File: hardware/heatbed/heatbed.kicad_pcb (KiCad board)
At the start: 2 copper layers, 200 x 200 mm, 4 parts, among them J1 Conn_01x01, J2 Conn_01x01

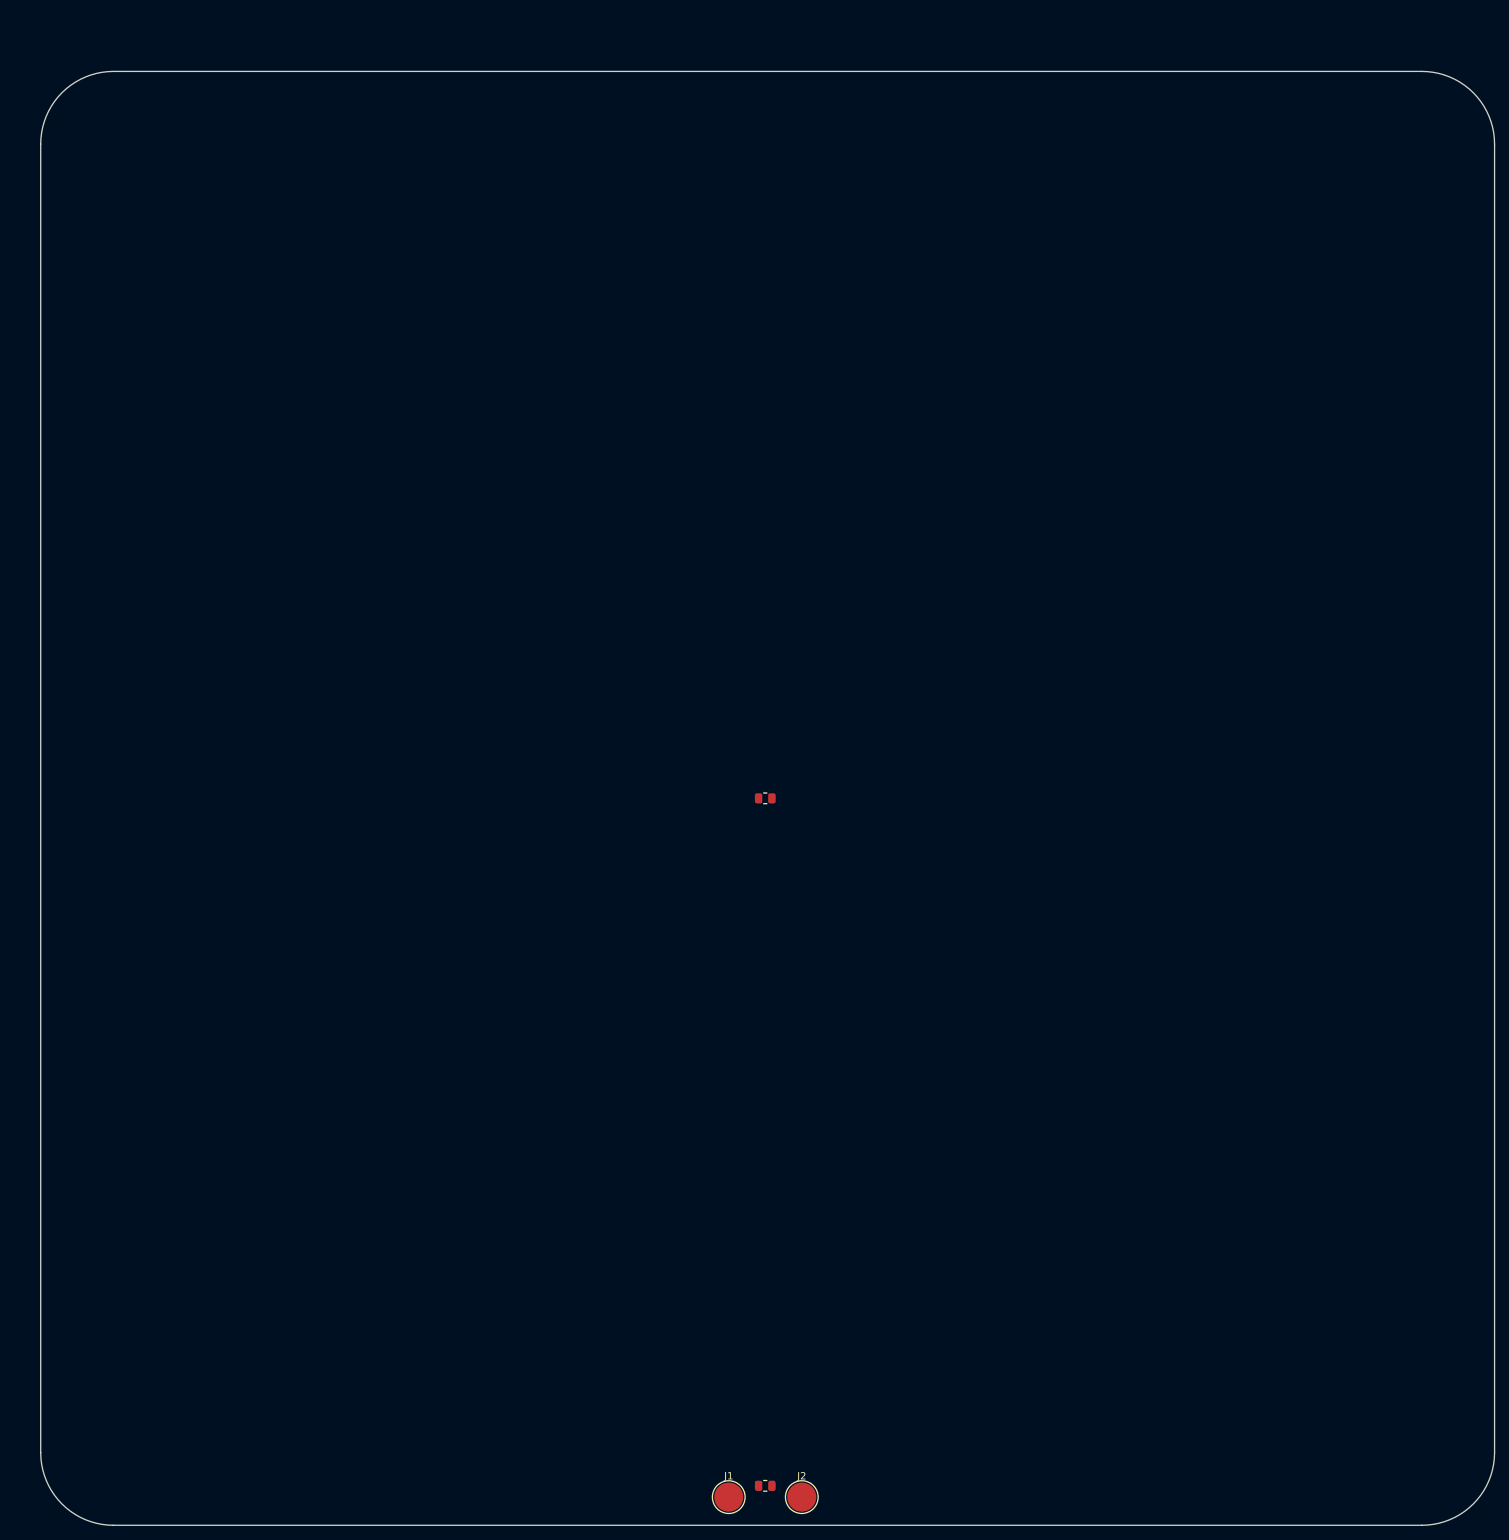
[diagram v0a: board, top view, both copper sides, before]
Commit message: add heatbed image
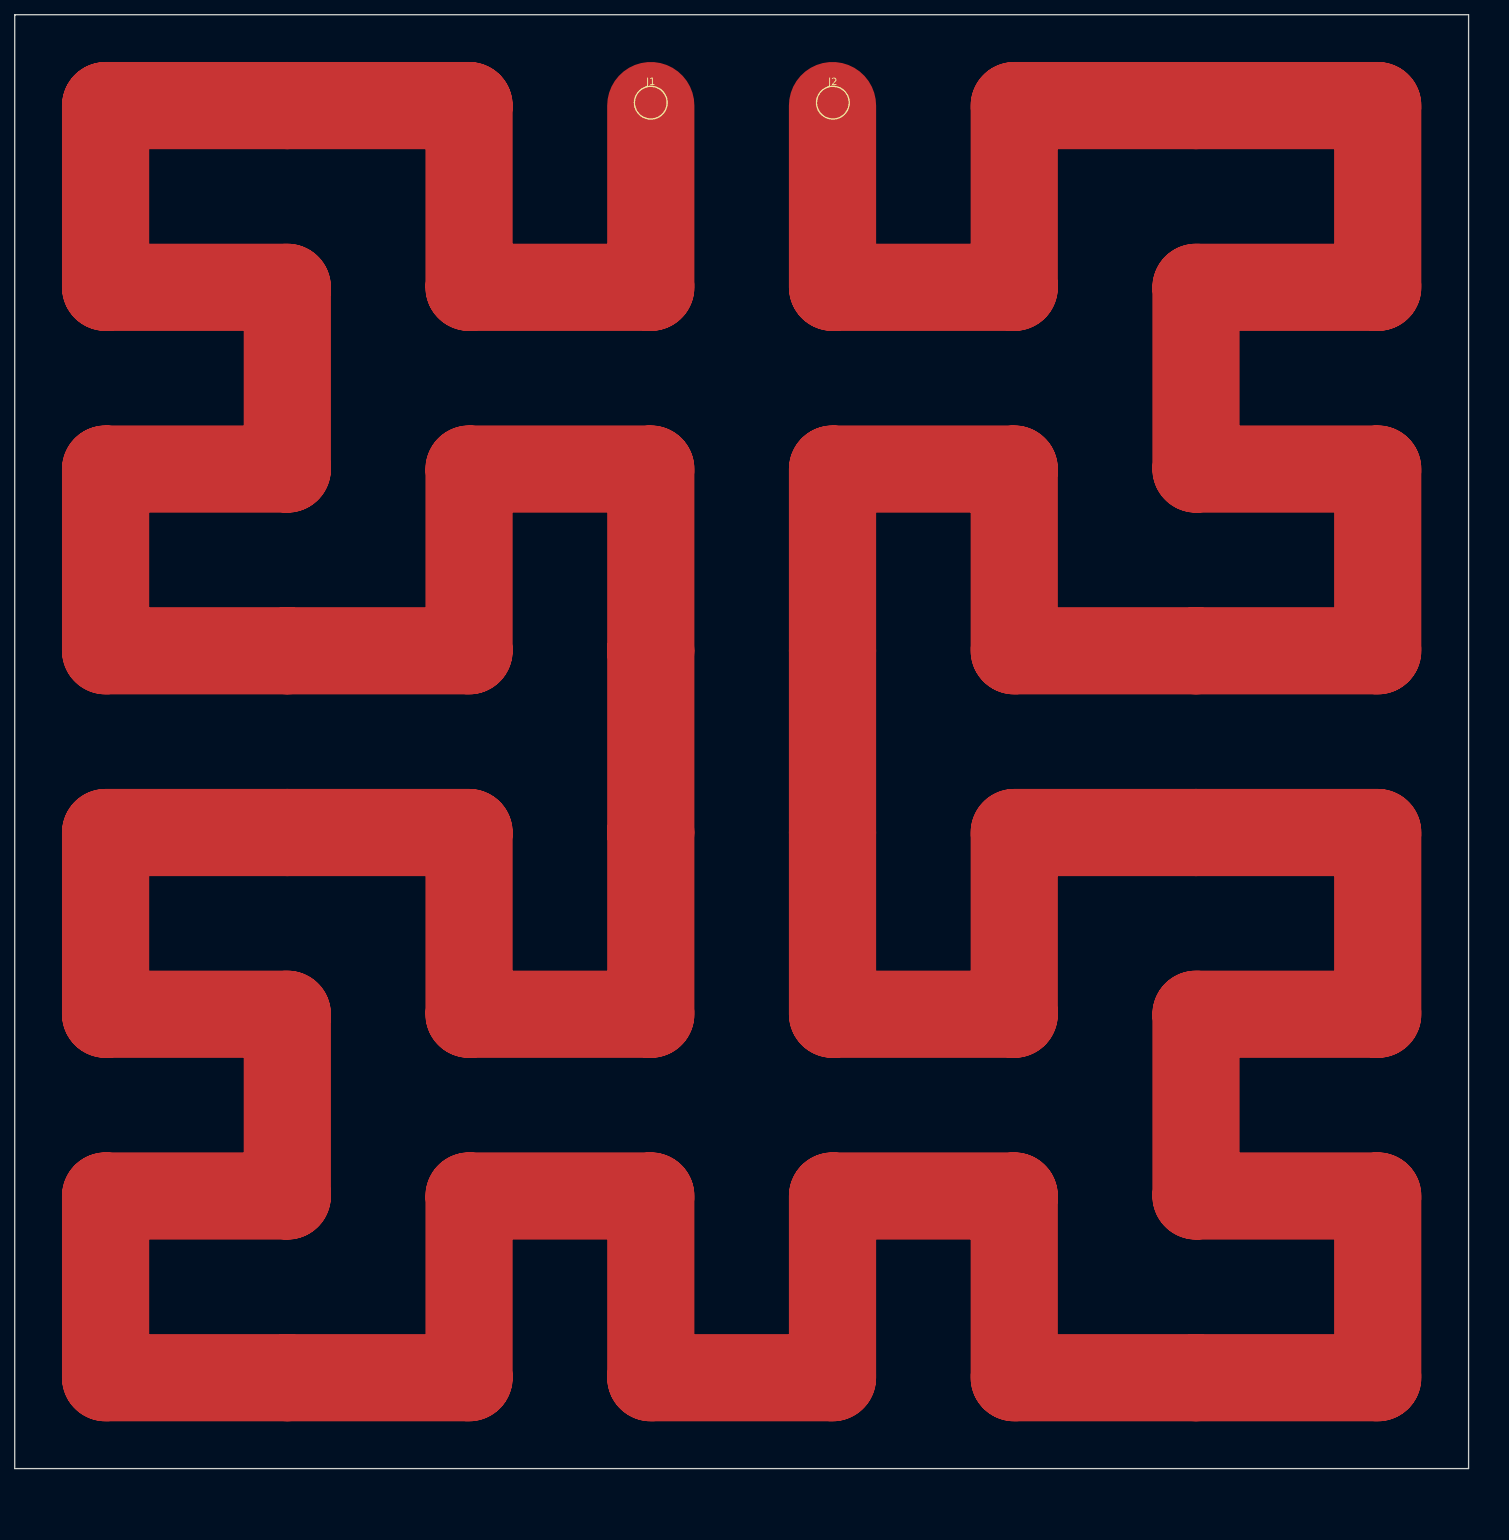
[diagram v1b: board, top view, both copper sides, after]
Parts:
- removed R1, R2: R, Resistor_SMD:R_0805_2012Metric
- moved J1 192.1 mm to (151.5, 58.5)
- moved J2 191.9 mm to (176.6, 58.5)
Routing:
- net Net-(J1-Pin_1): track 0.00 -> 1575.0 mm
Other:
- outline, holes or cut-outs redrawn

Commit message: fixed via sizing
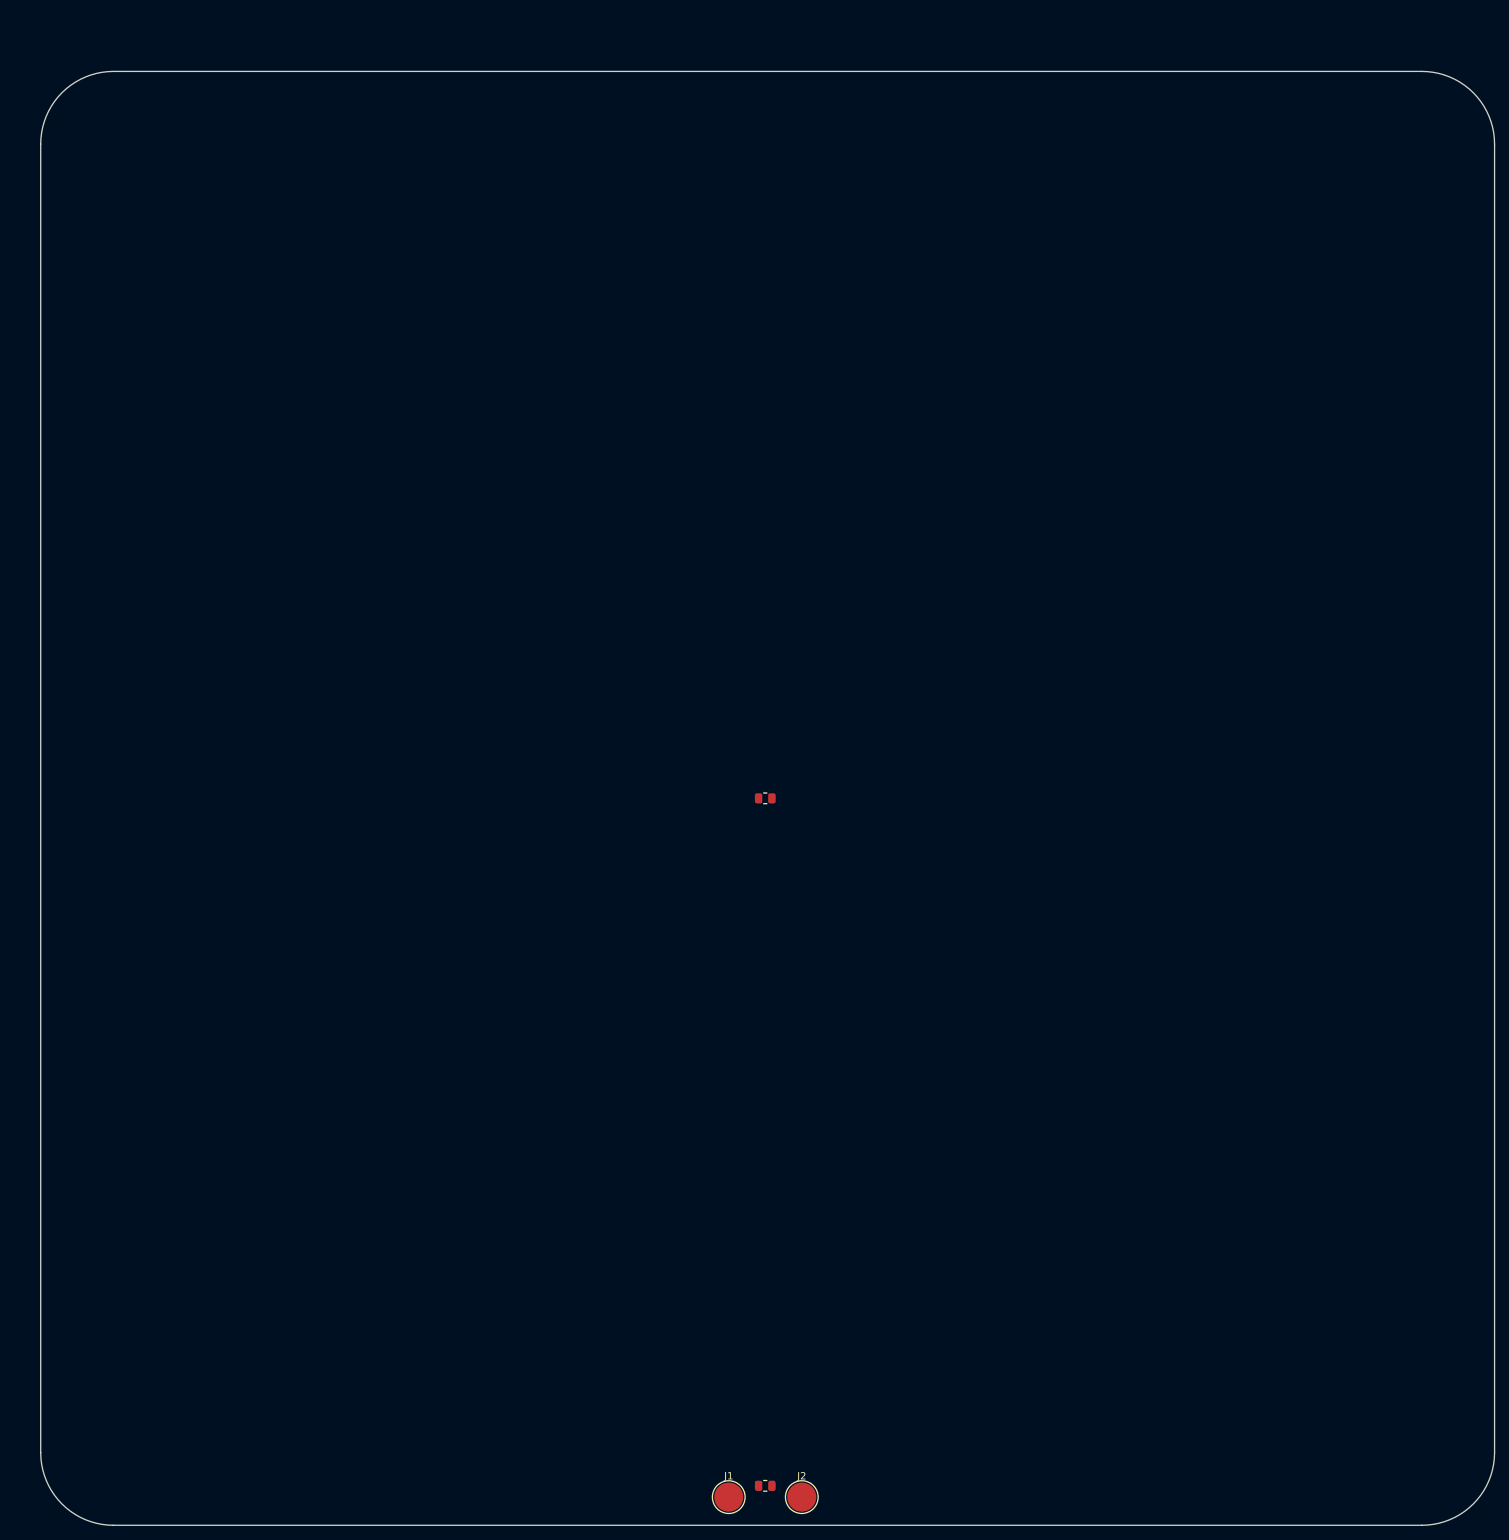
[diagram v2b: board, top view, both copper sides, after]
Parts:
- added R1: R, Resistor_SMD:R_0805_2012Metric, F.Cu at (167.3, 154.2)
- added R2: R, Resistor_SMD:R_0805_2012Metric, F.Cu at (167.3, 248.8)
- moved J1 192.1 mm to (162.2, 250.3)
- moved J2 191.9 mm to (172.3, 250.3)
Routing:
- net Net-(J1-Pin_1): track 1575.0 -> 0.00 mm
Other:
- outline, holes or cut-outs redrawn
